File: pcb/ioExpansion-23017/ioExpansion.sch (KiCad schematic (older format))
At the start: 12 parts, among them J1 GS3, J2 GS3, J3 GS3, U1 MCP23017, U2 Header2

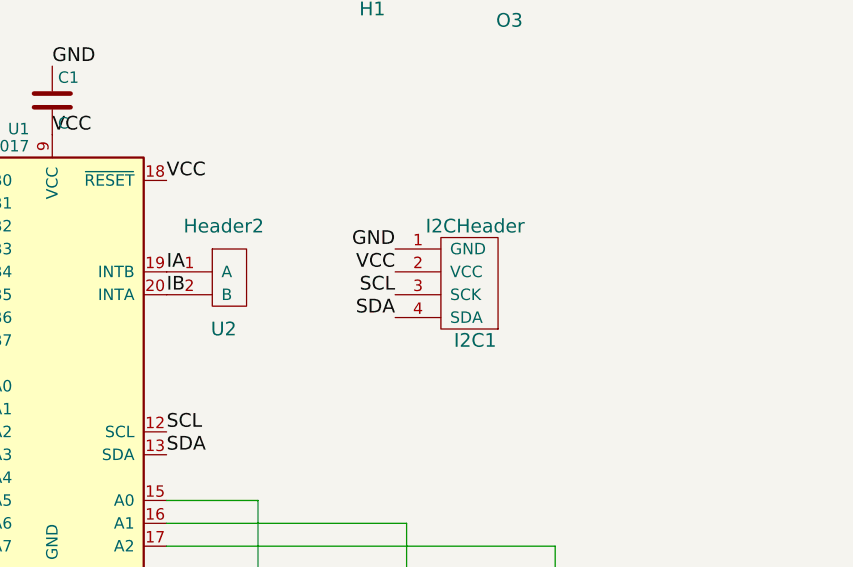
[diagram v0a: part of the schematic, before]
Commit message: Added extra I2C headers to the ioExpansion module.
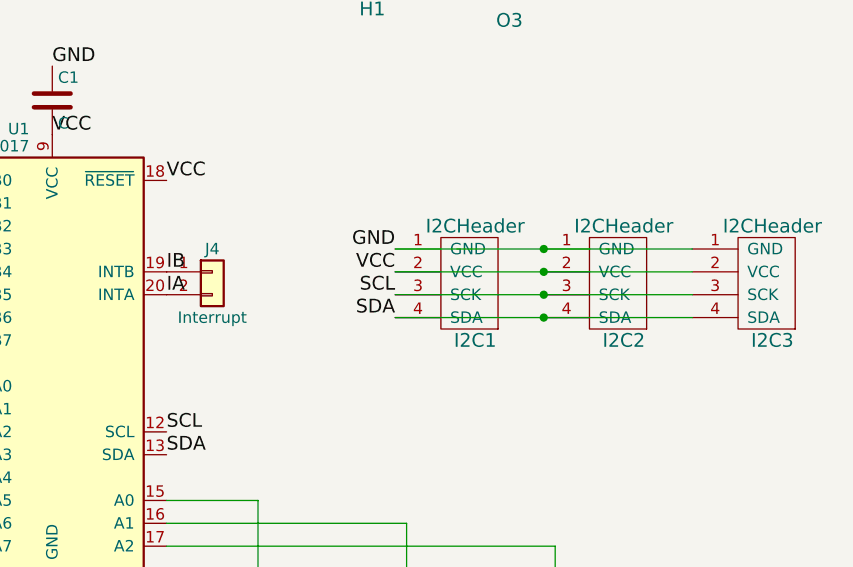
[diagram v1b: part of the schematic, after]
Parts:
- removed U2: Header2, Pin_Headers:Pin_Header_Straight_1x02_Pitch2.54mm, symbol Header2-RESCUE-MCP23017
- added I2C2, I2C3: I2CHeader, Pin_Headers:Pin_Header_Straight_1x04_Pitch2.54mm, symbol I2CHeader-RESCUE-MCP23017
- added J4: Interrupt, Pin_Headers:Pin_Header_Straight_1x02_Pitch2.54mm, symbol Conn_01x02
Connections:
- net GND: now also I2C2.1 (GND), I2C3.1 (GND)
- net IA: now also U1.20 (INTA), J4.2 (Pin_2); no longer U1.19 (INTB)
- net IB: now also U1.19 (INTB), J4.1 (Pin_1); no longer U1.20 (INTA)
- net L4: now also I2C2.4 (SDA), I2C3.4 (SDA)
- net L5: now also I2C2.3 (SCK), I2C3.3 (SCK)
- net VCC: now also I2C2.2 (VCC), I2C3.2 (VCC)
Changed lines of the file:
@@
 LIBS:eplay
 LIBS:Switch
-LIBS:MCP23017-cache
+LIBS:ioExpansion-cache
 EELAYER 25 0
 EELAYER END
@@
 Text Label 5900 4150 2    60   ~ 0
 GND
-$Comp
-L Header2-RESCUE-MCP23017 U2
-U 1 1 5AC33FEE
-P 5150 4150
-F 0 "U2" H 5150 3800 60  0000 C CNN
-F 1 "Header2" H 5150 4250 60  0000 C CNN
-F 2 "Pin_Headers:Pin_Header_Straight_1x02_Pitch2.54mm" H 5150 4150 60  0001 C CNN
-F 3 "" H 5150 4150 60  0001 C CNN
-	1    5150 4150
-	1    0    0    -1
-$EndComp
 $Comp
 L Headers8 H1
@@
 Wire Wire Line
 	3700 4550 3700 3700
+Text Label 4900 4250 0    60   ~ 0
+IB
 Text Label 4900 4350 0    60   ~ 0
-IB
-Text Label 4900 4250 0    60   ~ 0
 IA
+$Comp
+L Conn_01x02 J4
+U 1 1 5AE71117
+P 5100 4250
+F 0 "J4" H 5100 4350 50  0000 C CNN
+F 1 "Interrupt" H 5100 4050 50  0000 C CNN
+F 2 "Pin_Headers:Pin_Header_Straight_1x02_Pitch2.54mm" H 5100 4250 50  0001 C CNN
+F 3 "" H 5100 4250 50  0001 C CNN
+	1    5100 4250
+	1    0    0    -1
+$EndComp
+$Comp
+L I2CHeader-RESCUE-MCP23017 I2C2
+U 1 1 5AE715A1
+P 6750 4150
+F 0 "I2C2" H 6900 3750 60  0000 C CNN
+F 1 "I2CHeader" H 6900 4250 60  0000 C CNN
+F 2 "Pin_Headers:Pin_Header_Straight_1x04_Pitch2.54mm" H 6550 4200 60  0001 C CNN
+F 3 "" H 6550 4200 60  0001 C CNN
+	1    6750 4150
+	1    0    0    -1
+$EndComp
+Wire Wire Line
+	5900 4150 7200 4150
+Wire Wire Line
+	5900 4250 7200 4250
+Wire Wire Line
+	5900 4350 7200 4350
+Wire Wire Line
+	5900 4450 7200 4450
+$Comp
+L I2CHeader-RESCUE-MCP23017 I2C3
+U 1 1 5AE717BC
+P 7400 4150
+F 0 "I2C3" H 7550 3750 60  0000 C CNN
+F 1 "I2CHeader" H 7550 4250 60  0000 C CNN
+F 2 "Pin_Headers:Pin_Header_Straight_1x04_Pitch2.54mm" H 7200 4200 60  0001 C CNN
+F 3 "" H 7200 4200 60  0001 C CNN
+	1    7400 4150
+	1    0    0    -1
+$EndComp
+Connection ~ 6550 4150
+Connection ~ 6550 4250
+Connection ~ 6550 4350
+Connection ~ 6550 4450
 $EndSCHEMATC
